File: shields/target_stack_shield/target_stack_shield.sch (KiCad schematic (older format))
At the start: 7 parts

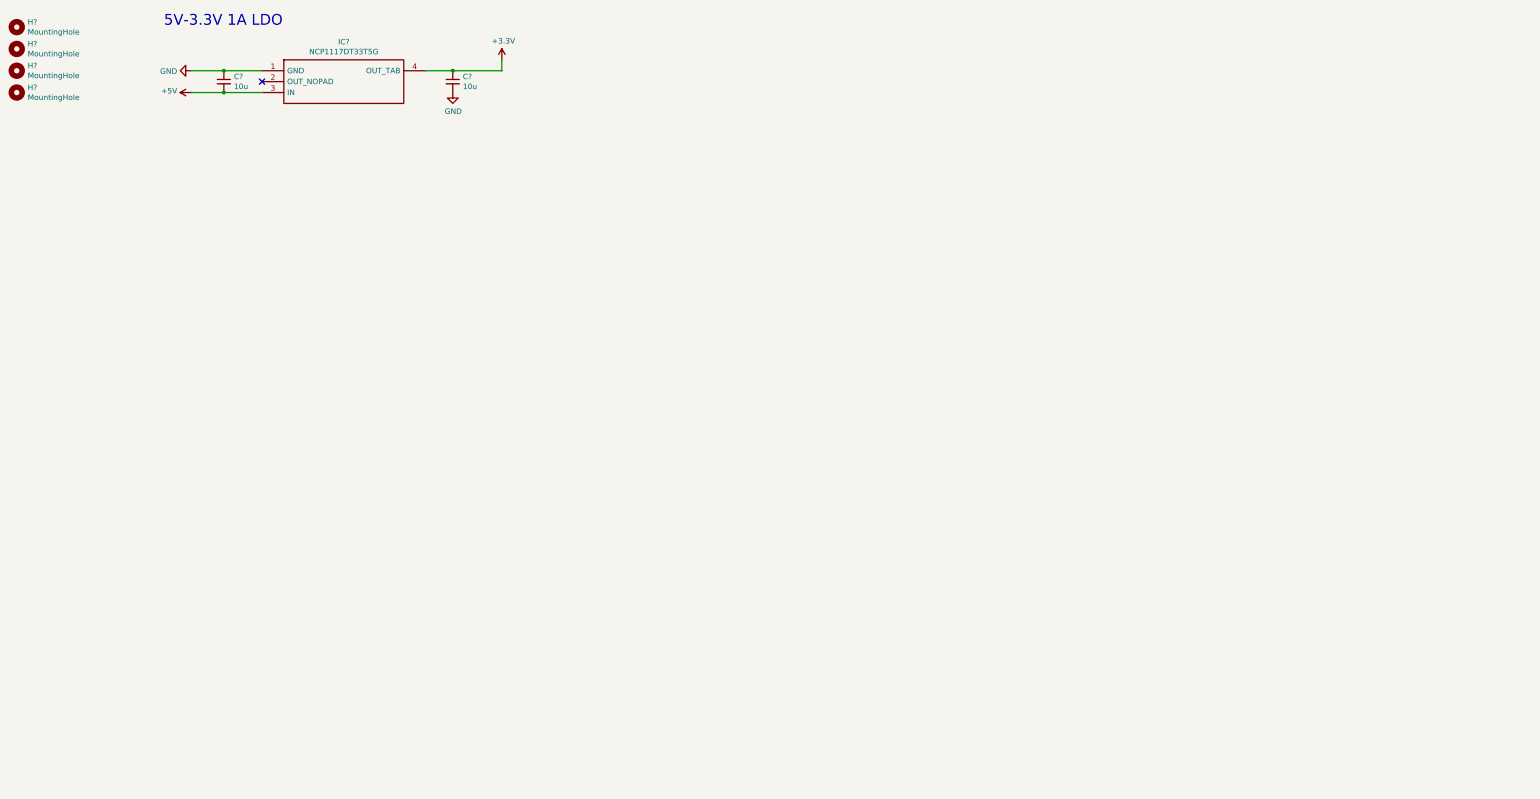
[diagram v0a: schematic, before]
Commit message: started with target stack shield schematics
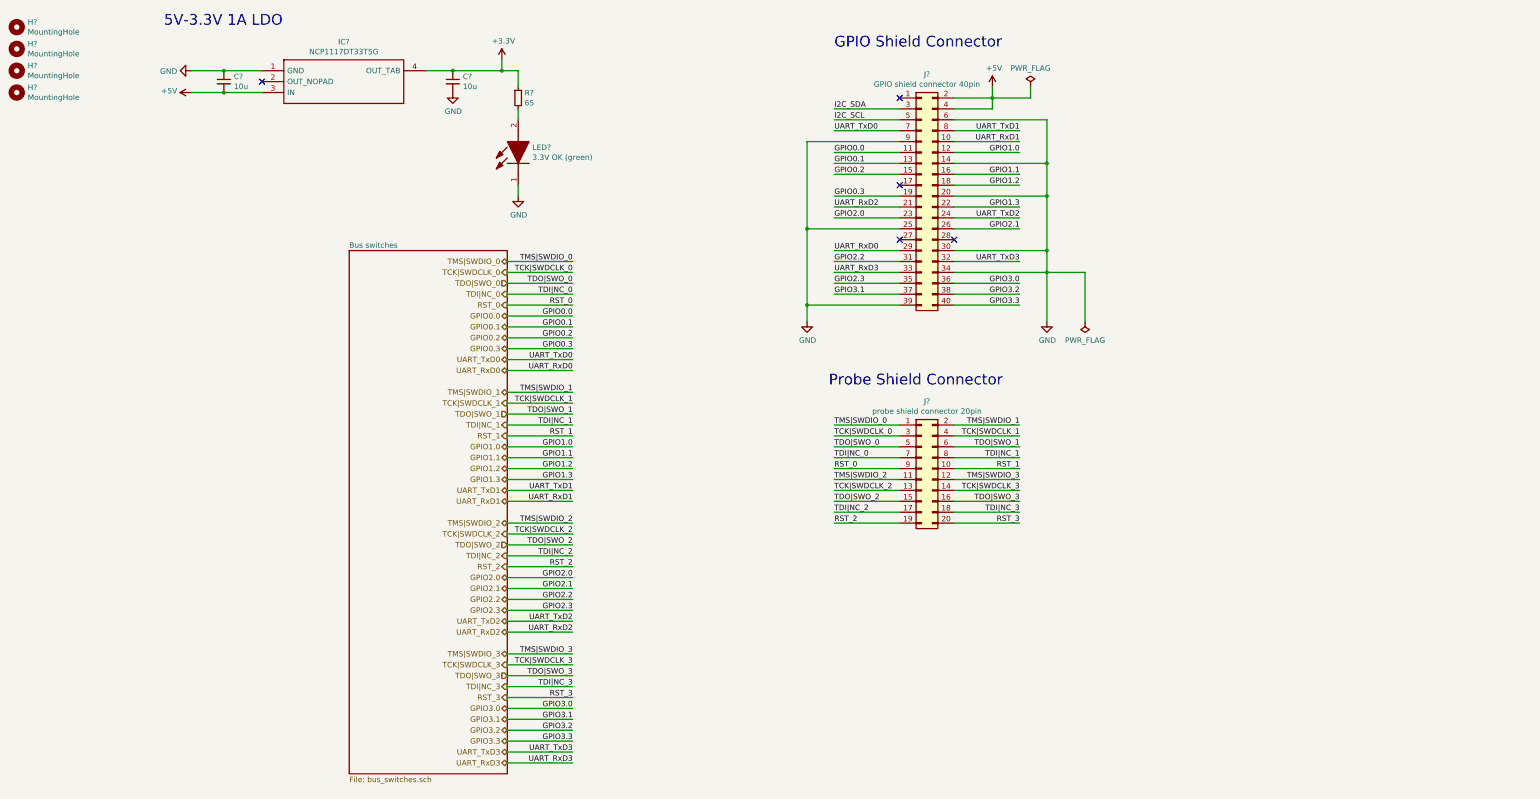
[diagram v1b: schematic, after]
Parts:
- added J?: GPIO shield connector 40pin, symbol Connector_Generic:Conn_02x20_Odd_Even
- added J?: probe shield connector 20pin, symbol Connector_Generic:Conn_02x10_Odd_Even
- added LED?: 3.3V OK (green), LEDC1608X80N, symbol hive:150060VS75000
- added R?: 65, symbol Device:R_Small
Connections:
- net +3V3: now also R?.1
- net +5V: now also J?.2 (Pin_2), J?.4 (Pin_4)
- net GND: now also J?.14 (Pin_14), J?.20 (Pin_20), J?.25 (Pin_25), J?.30 (Pin_30), J?.34 (Pin_34), J?.39 (Pin_39), J?.6 (Pin_6), J?.9 (Pin_9), LED?.1
- new net: LED?.2, R?.2
- new net GPIO0.0: J?.11 (Pin_11)
- new net GPIO0.1: J?.13 (Pin_13)
- new net GPIO0.2: J?.15 (Pin_15)
- new net GPIO0.3: J?.19 (Pin_19)
- new net GPIO1.0: J?.12 (Pin_12)
- new net GPIO1.1: J?.16 (Pin_16)
- new net GPIO1.2: J?.18 (Pin_18)
- new net GPIO1.3: J?.22 (Pin_22)
- new net GPIO2.0: J?.23 (Pin_23)
- new net GPIO2.1: J?.26 (Pin_26)
- new net GPIO2.2: J?.31 (Pin_31)
- new net GPIO2.3: J?.35 (Pin_35)
- new net GPIO3.0: J?.36 (Pin_36)
- new net GPIO3.1: J?.37 (Pin_37)
- new net GPIO3.2: J?.38 (Pin_38)
- new net GPIO3.3: J?.40 (Pin_40)
- new net I2C_SCL: J?.5 (Pin_5)
- new net I2C_SDA: J?.3 (Pin_3)
- new net RST_0: J?.9 (Pin_9)
- new net RST_1: J?.10 (Pin_10)
- new net RST_2: J?.19 (Pin_19)
- new net RST_3: J?.20 (Pin_20)
- new net TCK|SWDCLK_0: J?.3 (Pin_3)
- new net TCK|SWDCLK_1: J?.4 (Pin_4)
- new net TCK|SWDCLK_2: J?.13 (Pin_13)
- new net TCK|SWDCLK_3: J?.14 (Pin_14)
- new net TDI|NC_0: J?.7 (Pin_7)
- new net TDI|NC_1: J?.8 (Pin_8)
- new net TDI|NC_2: J?.17 (Pin_17)
- new net TDI|NC_3: J?.18 (Pin_18)
- new net TDO|SWO_0: J?.5 (Pin_5)
- new net TDO|SWO_1: J?.6 (Pin_6)
- new net TDO|SWO_2: J?.15 (Pin_15)
- new net TDO|SWO_3: J?.16 (Pin_16)
- new net TMS|SWDIO_0: J?.1 (Pin_1)
- new net TMS|SWDIO_1: J?.2 (Pin_2)
- new net TMS|SWDIO_2: J?.11 (Pin_11)
- new net TMS|SWDIO_3: J?.12 (Pin_12)
- new net UART_RxD0: J?.29 (Pin_29)
- new net UART_RxD1: J?.10 (Pin_10)
- new net UART_RxD2: J?.21 (Pin_21)
- new net UART_RxD3: J?.33 (Pin_33)
- new net UART_TxD0: J?.7 (Pin_7)
- new net UART_TxD1: J?.8 (Pin_8)
- new net UART_TxD2: J?.24 (Pin_24)
- new net UART_TxD3: J?.32 (Pin_32)
- no-connect marks 1 -> 5
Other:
- note added: "GPIO Shield Connector"
- note added: "Probe Shield Connector"

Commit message: further work on target stack shield schematics
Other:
- note added: "Daughterboard Connector"
- moved on the sheet: LED?

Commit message: schematic updates, start of probe shield layout
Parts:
- J?: value probe shield connector 20pin -> probe shield connector 20 or 26pin; symbol Connector_Generic:Conn_02x10_Odd_Even -> Connector_Generic:Conn_02x13_Odd_Even
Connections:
- net GND: now also J?.21 (Pin_21), J?.22 (Pin_22), J?.23 (Pin_23), J?.24 (Pin_24), J?.25 (Pin_25), J?.26 (Pin_26)
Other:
- note added: "Last 6 Pins are not required!\nYou may also use a 2x10pin \nconnector instead of a 2x13pin\nwith 2.54mm pitch"
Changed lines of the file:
@@
 Probe Shield Connector
 $Comp
-L Connector_Generic:Conn_02x10_Odd_Even J?
+L Connector_Generic:Conn_02x13_Odd_Even J?
 U 1 1 61503ABF
-P 9200 4850
-F 0 "J?" H 9250 5467 50  0000 C CNN
-F 1 "probe shield connector 20pin" H 9250 5376 50  0000 C CNN
-F 2 "" H 9200 4850 50  0001 C CNN
-F 3 "~" H 9200 4850 50  0001 C CNN
-	1    9200 4850
+P 9200 5050
+F 0 "J?" H 9250 5900 50  0000 C CNN
+F 1 "probe shield connector 20 or 26pin" H 9250 5800 50  0000 C CNN
+F 2 "" H 9200 5050 50  0001 C CNN
+F 3 "~" H 9200 5050 50  0001 C CNN
+	1    9200 5050
 	1    0    0    -1
 $EndComp
@@
 Text Notes 1200 2250 0    99   ~ 0
 Daughterboard Connector
+Wire Notes Line
+	9800 5800 8700 5800
+Wire Notes Line
+	8700 5800 8700 5400
+Wire Notes Line
+	8700 5400 9800 5400
+Wire Notes Line
+	9800 5400 9800 5800
+Wire Wire Line
+	9000 5450 8800 5450
+Wire Wire Line
+	8800 5450 8800 5550
+Wire Wire Line
+	8800 5750 9250 5750
+Wire Wire Line
+	9700 5750 9700 5650
+Wire Wire Line
+	9700 5450 9500 5450
+Wire Wire Line
+	9500 5550 9700 5550
+Connection ~ 9700 5550
+Wire Wire Line
+	9700 5550 9700 5450
+Wire Wire Line
+	9500 5650 9700 5650
+Connection ~ 9700 5650
+Wire Wire Line
+	9700 5650 9700 5550
+Wire Wire Line
+	9000 5550 8800 5550
+Connection ~ 8800 5550
+Wire Wire Line
+	8800 5550 8800 5650
+Wire Wire Line
+	9000 5650 8800 5650
+Connection ~ 8800 5650
+Wire Wire Line
+	8800 5650 8800 5750
+Wire Wire Line
+	9250 5750 9250 5900
+Connection ~ 9250 5750
+Wire Wire Line
+	9250 5750 9700 5750
+$Comp
+L power:GND #PWR?
+U 1 1 61589046
+P 9250 5900
+F 0 "#PWR?" H 9250 5650 50  0001 C CNN
+F 1 "GND" H 9255 5727 50  0000 C CNN
+F 2 "" H 9250 5900 50  0001 C CNN
+F 3 "" H 9250 5900 50  0001 C CNN
+	1    9250 5900
+	1    0    0    -1
+$EndComp
+Text Notes 9850 5750 0    50   ~ 0
+Last 6 Pins are not required!\nYou may also use a 2x10pin \nconnector instead of a 2x13pin\nwith 2.54mm pitch
 $EndSCHEMATC

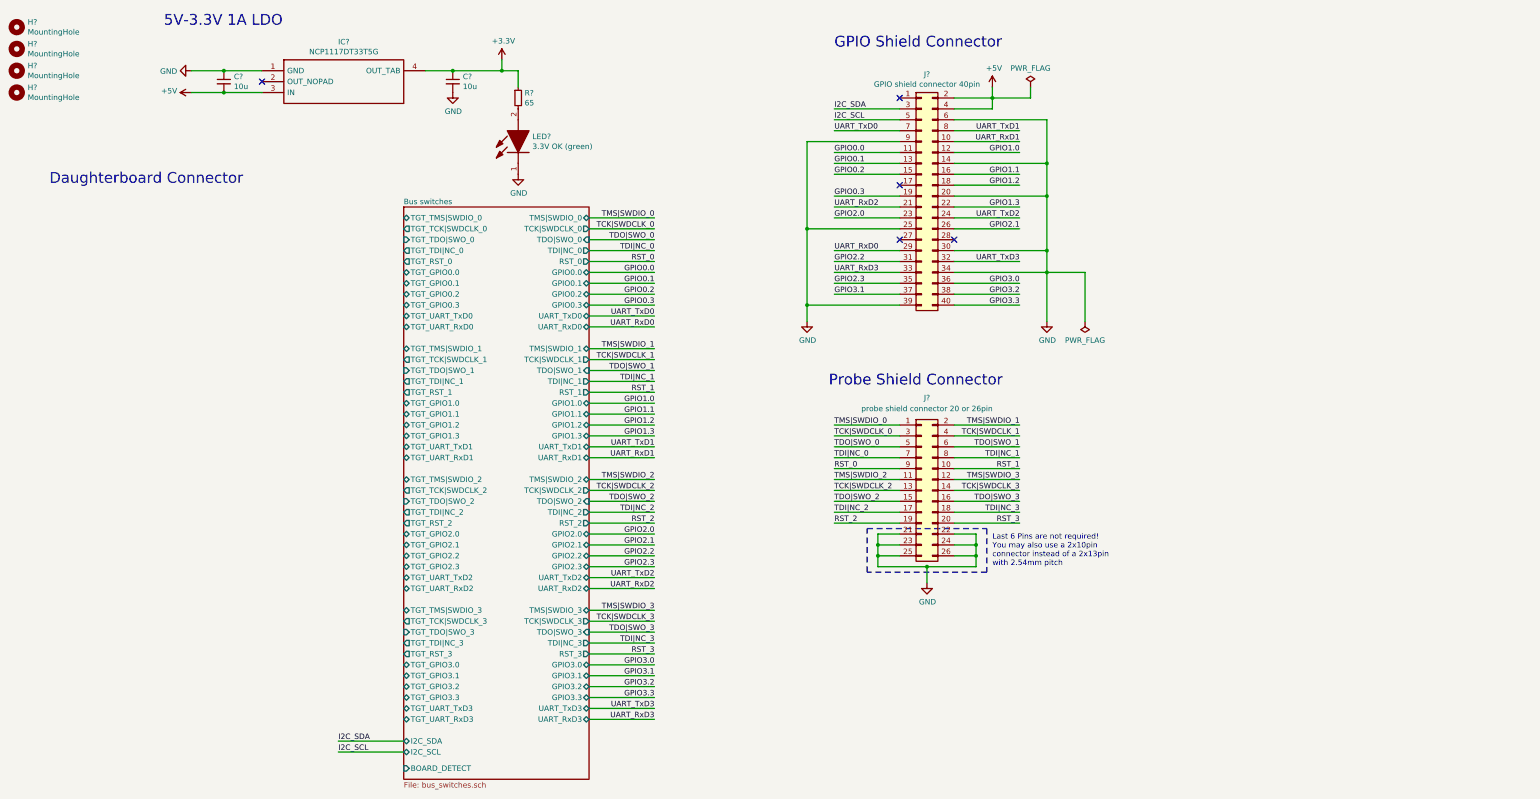
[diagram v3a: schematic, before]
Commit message: implemented changes according to feedback, finished target shield schematics
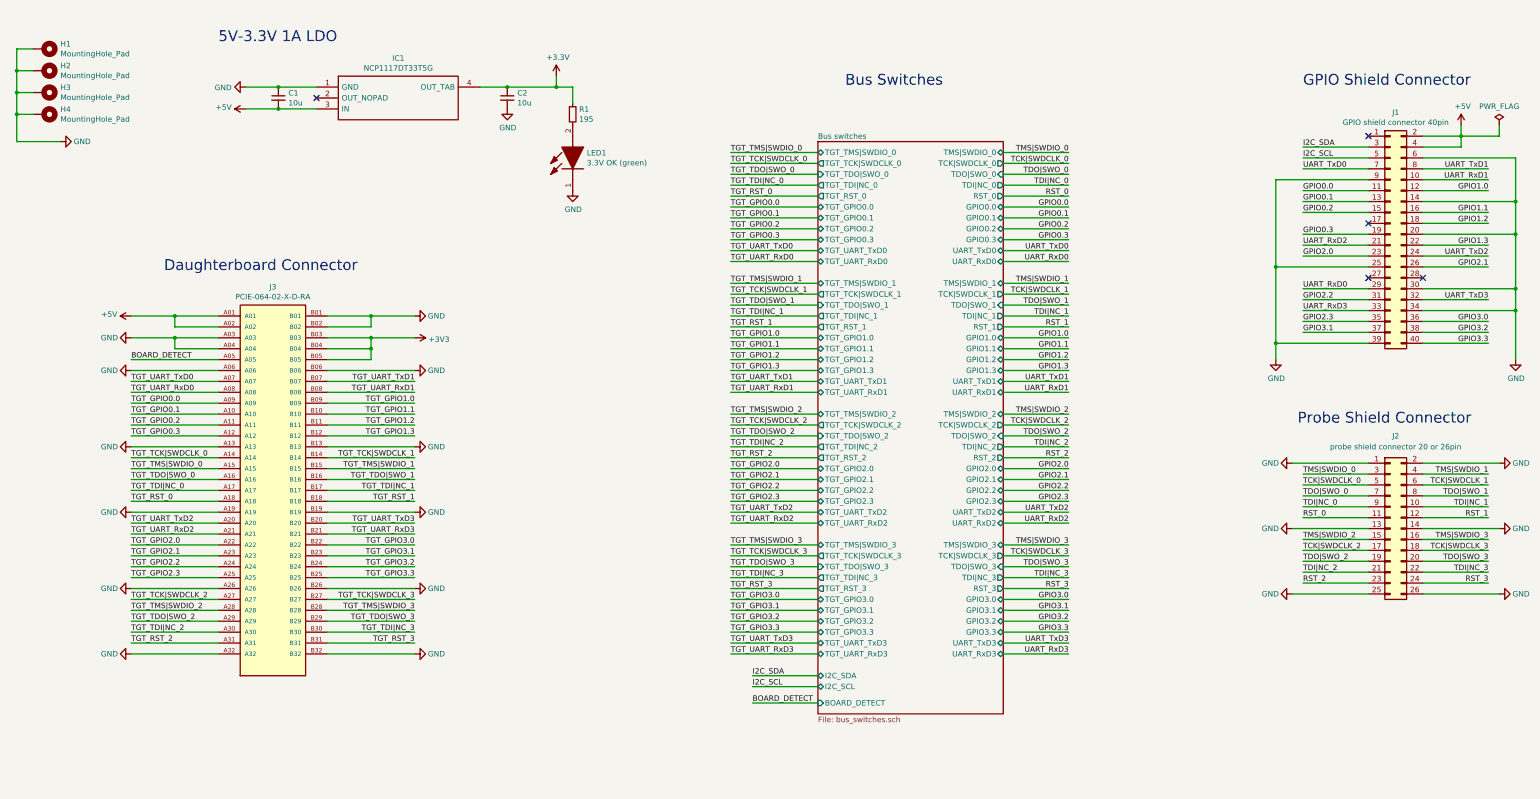
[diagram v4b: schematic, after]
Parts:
- removed H? (x4): MountingHole, symbol Mechanical:MountingHole
- added H1, H2, H3, H4: MountingHole_Pad, symbol Mechanical:MountingHole_Pad
- added J3: PCIE-064-02-X-D-RA, SAMTEC_PCIE-064-02-X-D-RA, symbol hive:PCIE-064-02-X-D-RA
- R1: renamed from R?; value 65 -> 195
- gave numbers to parts that had none: 6
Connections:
- net +3V3: now also J3.B03, J3.B04, J3.B05
- net +5V: now also J3.A01, J3.A02
- net GND: now also J2.1 (Pin_1), J2.13 (Pin_13), J2.14 (Pin_14), J2.2 (Pin_2), H1.1, H2.1, H3.1, H4.1, J3.A03, J3.A04, J3.A06, J3.A13, J3.A19, J3.A26, J3.A32, J3.B01, J3.B02, J3.B06, J3.B13, J3.B19, J3.B26, J3.B32; no longer J2.21 (Pin_21), J2.22 (Pin_22), J2.23 (Pin_23), J2.24 (Pin_24)
- net RST_0: now also J2.11 (Pin_11); no longer J2.9 (Pin_9)
- net RST_1: now also J2.12 (Pin_12); no longer J2.10 (Pin_10)
- net RST_2: now also J2.23 (Pin_23); no longer J2.19 (Pin_19)
- net RST_3: now also J2.24 (Pin_24); no longer J2.20 (Pin_20)
- net TCK|SWDCLK_0: now also J2.5 (Pin_5); no longer J2.3 (Pin_3)
- net TCK|SWDCLK_1: now also J2.6 (Pin_6); no longer J2.4 (Pin_4)
- net TCK|SWDCLK_2: now also J2.17 (Pin_17); no longer J2.13 (Pin_13)
- net TCK|SWDCLK_3: now also J2.18 (Pin_18); no longer J2.14 (Pin_14)
- net TDI|NC_0: now also J2.9 (Pin_9); no longer J2.7 (Pin_7)
- net TDI|NC_1: now also J2.10 (Pin_10); no longer J2.8 (Pin_8)
- net TDI|NC_2: now also J2.21 (Pin_21); no longer J2.17 (Pin_17)
- net TDI|NC_3: now also J2.22 (Pin_22); no longer J2.18 (Pin_18)
- net TDO|SWO_0: now also J2.7 (Pin_7); no longer J2.5 (Pin_5)
- net TDO|SWO_1: now also J2.8 (Pin_8); no longer J2.6 (Pin_6)
- net TDO|SWO_2: now also J2.19 (Pin_19); no longer J2.15 (Pin_15)
- net TDO|SWO_3: now also J2.20 (Pin_20); no longer J2.16 (Pin_16)
- net TMS|SWDIO_0: now also J2.3 (Pin_3); no longer J2.1 (Pin_1)
- net TMS|SWDIO_1: now also J2.4 (Pin_4); no longer J2.2 (Pin_2)
- net TMS|SWDIO_2: now also J2.15 (Pin_15); no longer J2.11 (Pin_11)
- net TMS|SWDIO_3: now also J2.16 (Pin_16); no longer J2.12 (Pin_12)
- new net BOARD_DETECT: J3.A05
- new net TGT_GPIO0.0: J3.A09
- new net TGT_GPIO0.1: J3.A10
- new net TGT_GPIO0.2: J3.A11
- new net TGT_GPIO0.3: J3.A12
- new net TGT_GPIO1.0: J3.B09
- new net TGT_GPIO1.1: J3.B10
- new net TGT_GPIO1.2: J3.B11
- new net TGT_GPIO1.3: J3.B12
- new net TGT_GPIO2.0: J3.A22
- new net TGT_GPIO2.1: J3.A23
- new net TGT_GPIO2.2: J3.A24
- new net TGT_GPIO2.3: J3.A25
- new net TGT_GPIO3.0: J3.B22
- new net TGT_GPIO3.1: J3.B23
- new net TGT_GPIO3.2: J3.B24
- new net TGT_GPIO3.3: J3.B25
- new net TGT_RST_0: J3.A18
- new net TGT_RST_1: J3.B18
- new net TGT_RST_2: J3.A31
- new net TGT_RST_3: J3.B31
- new net TGT_TCK|SWDCLK_0: J3.A14
- new net TGT_TCK|SWDCLK_1: J3.B14
- new net TGT_TCK|SWDCLK_2: J3.A27
- new net TGT_TCK|SWDCLK_3: J3.B27
- new net TGT_TDI|NC_0: J3.A17
- new net TGT_TDI|NC_1: J3.B17
- new net TGT_TDI|NC_2: J3.A30
- new net TGT_TDI|NC_3: J3.B30
- new net TGT_TDO|SWO_0: J3.A16
- new net TGT_TDO|SWO_1: J3.B16
- new net TGT_TDO|SWO_2: J3.A29
- new net TGT_TDO|SWO_3: J3.B29
- new net TGT_TMS|SWDIO_0: J3.A15
- new net TGT_TMS|SWDIO_1: J3.B15
- new net TGT_TMS|SWDIO_2: J3.A28
- new net TGT_TMS|SWDIO_3: J3.B28
- new net TGT_UART_RxD0: J3.A08
- new net TGT_UART_RxD1: J3.B08
- new net TGT_UART_RxD2: J3.A21
- new net TGT_UART_RxD3: J3.B21
- new net TGT_UART_TxD0: J3.A07
- new net TGT_UART_TxD1: J3.B07
- new net TGT_UART_TxD2: J3.A20
- new net TGT_UART_TxD3: J3.B20
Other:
- note added: "Bus Switches"
- note removed: "Last 6 Pins are not required!\nYou may also use a 2x10pin \nconnector instead of a 2x13pin\nwith 2.54mm pitch"
- moved on the sheet: C1, C2, IC1, J1, J2, LED1, R1

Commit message: work on target stack shield layout
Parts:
- C1, C2: footprint (none) -> Capacitor_SMD:C_0805_2012Metric_Pad1.15x1.40mm_HandSolder
- H1, H2, H3, H4: footprint (none) -> MountingHole:MountingHole_2.7mm_M2.5_DIN965_Pad
- IC1: footprint TO229P990X238-4N -> hive:TO229P990X238-4N
- J1: footprint (none) -> hive:PinHeader_2x20_P2.54mm_Vertical_gpio_shield
- J2: value probe shield connector 20 or 26pin -> probe shield connector 26pin; footprint (none) -> hive:PinHeader_2x13_P2.54mm_Vertical_probe_shield
- J3: footprint SAMTEC_PCIE-064-02-X-D-RA -> hive:SAMTEC_PCIE-064-02-X-D-RA
- LED1: footprint LEDC1608X80N -> hive:LEDC1608X80N
- R1: footprint (none) -> Resistor_SMD:R_0603_1608Metric_Pad1.05x0.95mm_HandSolder
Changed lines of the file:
@@
 F 0 "IC1" H 4400 1615 50  0000 C CNN
 F 1 "NCP1117DT33T5G" H 4400 1524 50  0000 C CNN
-F 2 "TO229P990X238-4N" H 5000 1450 50  0001 L CNN
+F 2 "hive:TO229P990X238-4N" H 5000 1450 50  0001 L CNN
 F 3 "http://www.onsemi.com/pub/Collateral/NCP1117-D.PDF" H 5000 1350 50  0001 L CNN
 F 4 "2.38" H 5000 1150 50  0001 L CNN "Height"
@@
 F 0 "C1" H 3392 1496 50  0000 L CNN
 F 1 "10u" H 3392 1405 50  0000 L CNN
-F 2 "" H 3300 1450 50  0001 C CNN
+F 2 "Capacitor_SMD:C_0805_2012Metric_Pad1.15x1.40mm_HandSolder" H 3300 1450 50  0001 C CNN
 F 3 "~" H 3300 1450 50  0001 C CNN
 	1    3300 1450
@@
 F 0 "C2" H 5492 1496 50  0000 L CNN
 F 1 "10u" H 5492 1405 50  0000 L CNN
-F 2 "" H 5400 1450 50  0001 C CNN
+F 2 "Capacitor_SMD:C_0805_2012Metric_Pad1.15x1.40mm_HandSolder" H 5400 1450 50  0001 C CNN
 F 3 "~" H 5400 1450 50  0001 C CNN
 	1    5400 1450
@@
 F 0 "R1" H 6059 1646 50  0000 L CNN
 F 1 "195" H 6059 1555 50  0000 L CNN
-F 2 "" H 6000 1600 50  0001 C CNN
+F 2 "Resistor_SMD:R_0603_1608Metric_Pad1.05x0.95mm_HandSolder" H 6000 1600 50  0001 C CNN
 F 3 "~" H 6000 1600 50  0001 C CNN
 	1    6000 1600
@@
 F 0 "LED1" V 6346 2170 50  0000 R CNN
 F 1 "3.3V OK (green)" V 6255 2170 50  0000 R CNN
-F 2 "LEDC1608X80N" H 6500 2450 50  0001 L BNN
+F 2 "hive:LEDC1608X80N" H 6500 2450 50  0001 L BNN
 F 3 "https://componentsearchengine.com/Datasheets/2/150060VS75000.pdf" H 6500 2350 50  0001 L BNN
 F 4 "2.4 V Green LED 1608 (0603) SMD, Wurth Elektronik WL-SMCW 150060VS75000" H 6500 2250 50  0001 L BNN "Description"
@@
 F 0 "J1" H 13550 3817 50  0000 C CNN
 F 1 "GPIO shield connector 40pin" H 13550 3726 50  0000 C CNN
-F 2 "" H 13500 2700 50  0001 C CNN
+F 2 "hive:PinHeader_2x20_P2.54mm_Vertical_gpio_shield" H 13500 2700 50  0001 C CNN
 F 3 "~" H 13500 2700 50  0001 C CNN
 	1    13500 2700
@@
 P 13500 5400
 F 0 "J2" H 13550 6250 50  0000 C CNN
-F 1 "probe shield connector 20 or 26pin" H 13550 6150 50  0000 C CNN
-F 2 "" H 13500 5400 50  0001 C CNN
+F 1 "probe shield connector 26pin" H 13550 6150 50  0000 C CNN
+F 2 "hive:PinHeader_2x13_P2.54mm_Vertical_probe_shield" H 13500 5400 50  0001 C CNN
 F 3 "~" H 13500 5400 50  0001 C CNN
 	1    13500 5400
@@
 F 0 "J3" H 3250 6917 50  0000 C CNN
 F 1 "PCIE-064-02-X-D-RA" H 3250 6826 50  0000 C CNN
-F 2 "SAMTEC_PCIE-064-02-X-D-RA" H 3250 5050 50  0001 L BNN
+F 2 "hive:SAMTEC_PCIE-064-02-X-D-RA" H 3250 5050 50  0001 L BNN
 F 3 "" H 3250 5050 50  0001 L BNN
 F 4 "Samtec Inc" H 3250 5050 50  0001 L BNN "MANUFACTURER"
@@
 F 0 "H1" V 1104 1150 50  0000 L CNN
 F 1 "MountingHole_Pad" V 1195 1150 50  0000 L CNN
-F 2 "" H 1150 1000 50  0001 C CNN
+F 2 "MountingHole:MountingHole_2.7mm_M2.5_DIN965_Pad" H 1150 1000 50  0001 C CNN
 F 3 "~" H 1150 1000 50  0001 C CNN
 	1    1150 1000
@@
 F 0 "H2" V 1104 1350 50  0000 L CNN
 F 1 "MountingHole_Pad" V 1195 1350 50  0000 L CNN
-F 2 "" H 1150 1200 50  0001 C CNN
+F 2 "MountingHole:MountingHole_2.7mm_M2.5_DIN965_Pad" H 1150 1200 50  0001 C CNN
 F 3 "~" H 1150 1200 50  0001 C CNN
 	1    1150 1200
@@
 F 0 "H3" V 1104 1550 50  0000 L CNN
 F 1 "MountingHole_Pad" V 1195 1550 50  0000 L CNN
-F 2 "" H 1150 1400 50  0001 C CNN
+F 2 "MountingHole:MountingHole_2.7mm_M2.5_DIN965_Pad" H 1150 1400 50  0001 C CNN
 F 3 "~" H 1150 1400 50  0001 C CNN
 	1    1150 1400
@@
 F 0 "H4" V 1104 1750 50  0000 L CNN
 F 1 "MountingHole_Pad" V 1195 1750 50  0000 L CNN
-F 2 "" H 1150 1600 50  0001 C CNN
+F 2 "MountingHole:MountingHole_2.7mm_M2.5_DIN965_Pad" H 1150 1600 50  0001 C CNN
 F 3 "~" H 1150 1600 50  0001 C CNN
 	1    1150 1600
